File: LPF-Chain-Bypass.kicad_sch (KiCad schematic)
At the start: 2 parts, among them K1 HK19F-DCxxV-SHC, K2 HK19F-DCxxV-SHC

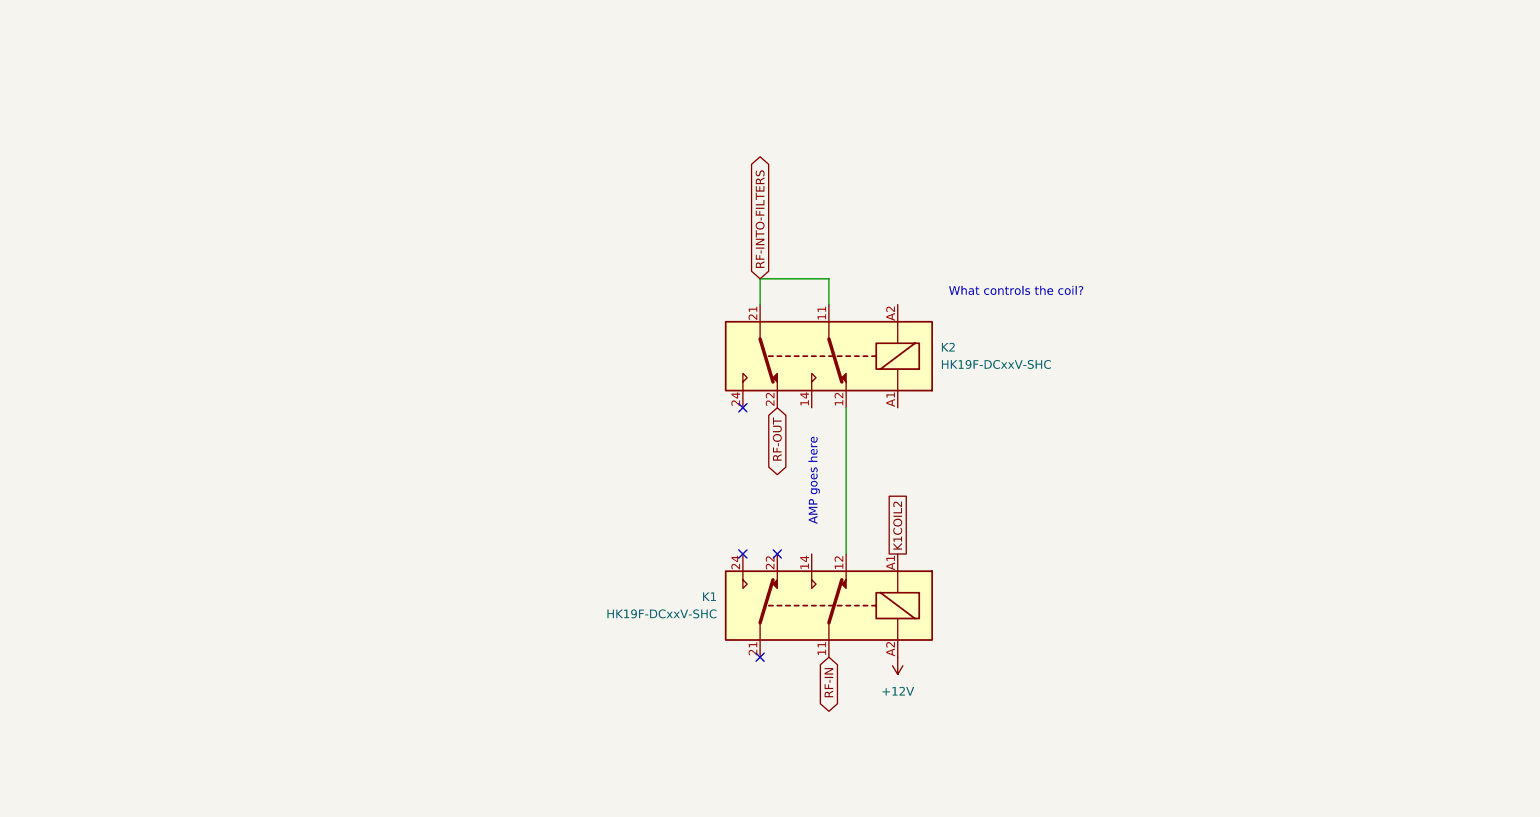
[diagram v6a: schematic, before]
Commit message: added cap values to filter chain per Ron
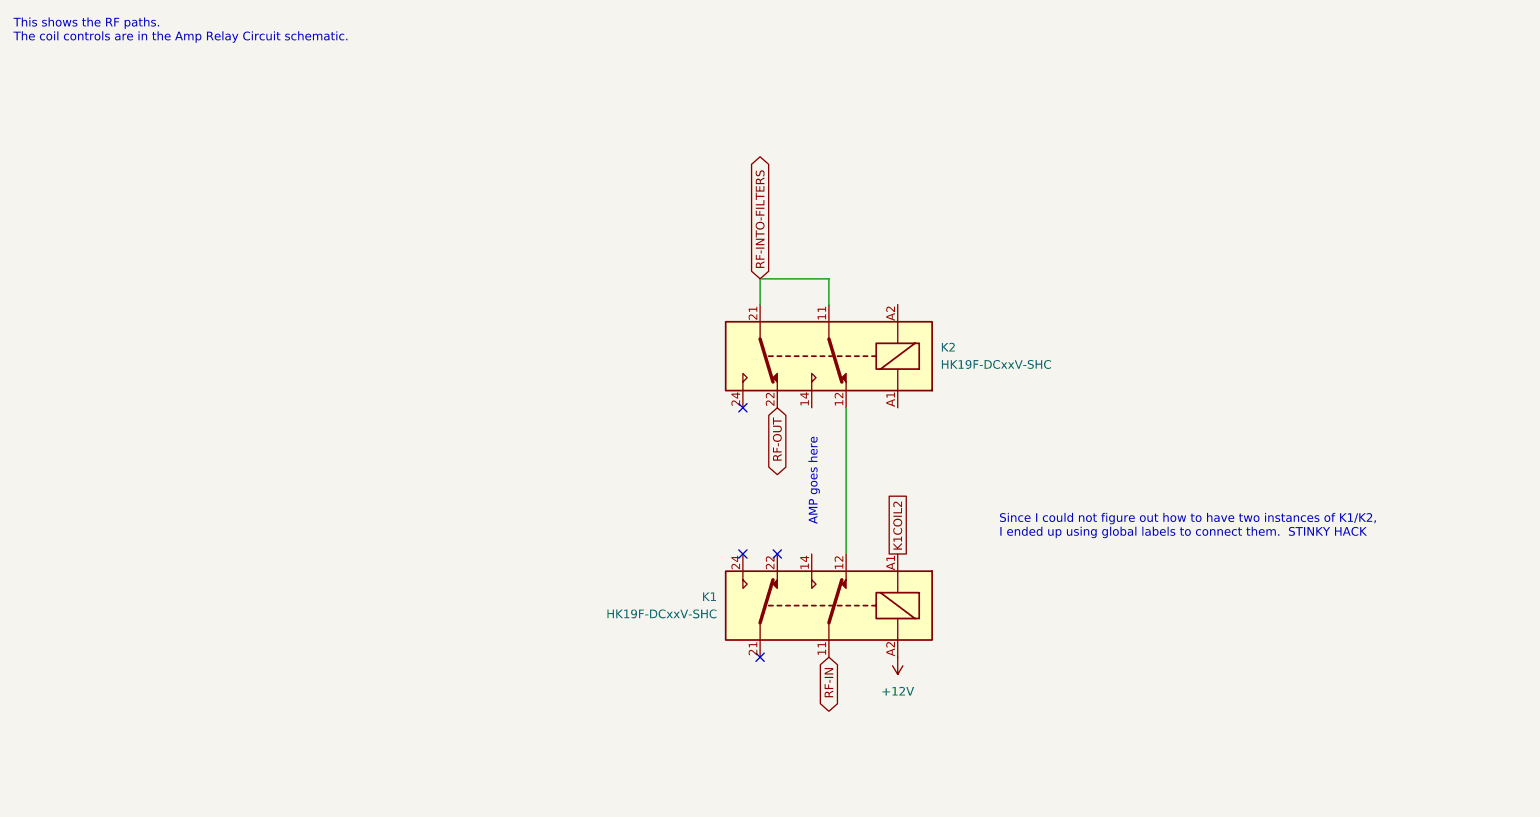
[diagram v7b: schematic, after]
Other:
- note added: "Since I could not figure out how to have two instances of K1/K2, I ended up using global labels to connect them. STINKY HACK"
- note added: "This shows the RF paths. The coil controls are in the Amp Relay Circuit schematic."
- note removed: "What controls the coil?"
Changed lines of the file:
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@@
 	(title_block
 		(title "QMX Amp")
-		(date "2024-08-10")
+		(date "2024-08-11")
 		(rev "v0.2")
 		(company "WA7GIL")
@@
 		)
 	)
-	(text "What controls the coil?"
+	(text "Since I could not figure out how to have two instances of K1/K2,\nI ended up using global labels to connect them.  STINKY HACK"
 		(exclude_from_sim no)
-		(at 168.656 61.722 0)
+		(at 166.116 96.266 0)
 		(effects
 			(font
 				(size 1.27 1.27)
 			)
+			(justify left)
 		)
 	)
+	(text "This shows the RF paths.\nThe coil controls are in the Amp Relay Circuit schematic."
+		(exclude_from_sim no)
+		(at 20.574 23.114 0)
+		(effects
+			(font
+				(size 1.27 1.27)
+			)
+			(justify left)
+		)
+	)

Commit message: checkpoint progress from Sunday 240811
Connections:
- net K2-14: now reaches K2.14
- net K1-14: now reaches K1.14
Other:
- note removed: "AMP goes here"
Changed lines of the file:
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@@
 		(title "QMX Amp")
 		(date "2024-08-11")
-		(rev "v0.2")
+		(rev "v0.3")
 		(company "WA7GIL")
 	)
@@
 		)
 	)
-	(text "AMP goes here"
-		(exclude_from_sim no)
-		(at 138.684 89.662 90)
-		(effects
-			(font
-				(size 1.27 1.27)
-			)
-		)
-	)
 	(text "Since I could not figure out how to have two instances of K1/K2,\nI ended up using global labels to connect them.  STINKY HACK"
 		(exclude_from_sim no)
@@
 			)
 			(justify left)
+		)
+	)
+	(global_label "K2-14"
+		(shape bidirectional)
+		(at 138.43 78.74 270)
+		(fields_autoplaced yes)
+		(effects
+			(font
+				(size 1.27 1.27)
+			)
+			(justify right)
+		)
+		(property "Intersheetrefs" "${INTERSHEET_REFS}"
+			(at 138.43 89.3072 90)
+			(effects
+				(font
+					(size 1.27 1.27)
+				)
+				(justify right)
+				(hide yes)
+			)
 		)
 	)
@@
 			(effects
 				(font
+					(size 1.27 1.27)
+				)
+				(justify left)
+				(hide yes)
+			)
+		)
+	)
+	(global_label "K1-14"
+		(shape bidirectional)
+		(at 138.43 100.33 90)
+		(fields_autoplaced yes)
+		(effects
+			(font
+				(size 1.27 1.27)
+			)
+			(justify left)
+		)
+		(property "Intersheetrefs" "${INTERSHEET_REFS}"
+			(at 138.43 89.7628 90)
+			(effects
+				(font
